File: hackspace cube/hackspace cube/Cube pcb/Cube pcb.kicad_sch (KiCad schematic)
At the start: 57 parts, among them J1 Conn_01x08 ( conector 1), J2 Conn_01x08 ( conector 2), J3 Conn_01x02 ( exstra ground co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, J4 Conn_01x14 ( Spare Ports ), Q1 BSS138, Q10 BSS138, Q11 BSS138, Q12 BSS138, Q13 BSS138, Q14 BSS138, Q15 BSS138, Q16 BSS138, Q2 BSS138, Q3 BSS138, Q4 BSS138, Q5 BSS138, Q6 BSS138, Q7 BSS138, Q8 BSS138, Q9 BSS138

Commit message: update
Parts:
- C1, C2, C3, C4: footprint Capacitor_SMD:C_0805_2012Metric -> (none)
- J1, J2: footprint Connector_PinHeader_2.54mm:PinHeader_1x08_P2.54mm_Vertical -> (none)
- J3: footprint Connector_PinHeader_2.54mm:PinHeader_1x02_P2.54mm_Vertical -> (none)
- J4: footprint Connector_PinHeader_2.54mm:PinHeader_1x14_P2.54mm_Vertical -> (none)
- R1, R10, R11, R12, R13, R14, R15, R16, R17, R18, R19, R2, R20, R21, R22, R23, R24, R25, R26, R27, R28, R29, R3, R30, R31, R32, R4, R5, R6, R7, R8, R9: footprint Resistor_SMD:R_0805_2012Metric -> (none)
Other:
- note added: "1.2"
- note removed: "1.1"
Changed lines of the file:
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@@
 		)
 	)
-	(text "1.1\n"
+	(text "1.2\n"
 		(exclude_from_sim no)
 		(at 270.256 193.294 0)
@@
 			)
 		)
-		(property "Footprint" "Capacitor_SMD:C_0805_2012Metric"
+		(property "Footprint" ""
 			(at 145.7452 41.91 0)
 			(effects
@@
 			)
 		)
-		(property "Footprint" "Capacitor_SMD:C_0805_2012Metric"
+		(property "Footprint" ""
 			(at 131.7752 41.91 0)
 			(effects
@@
 			)
 		)
-		(property "Footprint" "Resistor_SMD:R_0805_2012Metric"
+		(property "Footprint" ""
 			(at 24.892 163.83 90)
 			(effects
@@
 			)
 		)
-		(property "Footprint" "Resistor_SMD:R_0805_2012Metric"
+		(property "Footprint" ""
 			(at 45.212 163.83 90)
 			(effects
@@
 			)
 		)
-		(property "Footprint" "Resistor_SMD:R_0805_2012Metric"
+		(property "Footprint" ""
 			(at 51.562 26.67 90)
 			(effects
@@
 			)
 		)
-		(property "Footprint" "Connector_PinHeader_2.54mm:PinHeader_1x08_P2.54mm_Vertical"
+		(property "Footprint" ""
 			(at 162.56 85.09 0)
 			(effects
@@
 			)
 		)
-		(property "Footprint" "Connector_PinHeader_2.54mm:PinHeader_1x14_P2.54mm_Vertical"
+		(property "Footprint" ""
 			(at 248.92 135.89 0)
 			(effects
@@
 			)
 		)
-		(property "Footprint" "Resistor_SMD:R_0805_2012Metric"
+		(property "Footprint" ""
 			(at 68.072 88.9 90)
 			(effects
@@
 			)
 		)
-		(property "Footprint" "Resistor_SMD:R_0805_2012Metric"
+		(property "Footprint" ""
 			(at 51.562 44.45 90)
 			(effects
@@
 			)
 		)
-		(property "Footprint" "Resistor_SMD:R_0805_2012Metric"
+		(property "Footprint" ""
 			(at 31.242 44.45 90)
 			(effects
@@
 			)
 		)
-		(property "Footprint" "Connector_PinHeader_2.54mm:PinHeader_1x02_P2.54mm_Vertical"
+		(property "Footprint" ""
 			(at 163.83 144.78 0)
 			(effects
@@
 			)
 		)
-		(property "Footprint" "Resistor_SMD:R_0805_2012Metric"
+		(property "Footprint" ""
 			(at 89.662 26.67 90)
 			(effects
@@
 			)
 		)
-		(property "Footprint" "Resistor_SMD:R_0805_2012Metric"
+		(property "Footprint" ""
 			(at 29.972 134.62 90)
 			(effects
@@
 			)
 		)
-		(property "Footprint" "Resistor_SMD:R_0805_2012Metric"
+		(property "Footprint" ""
 			(at 87.122 88.9 90)
 			(effects
@@
 			)
 		)
-		(property "Footprint" "Resistor_SMD:R_0805_2012Metric"
+		(property "Footprint" ""
 			(at 49.022 88.9 90)
 			(effects
@@
 			)
 		)
-		(property "Footprint" "Resistor_SMD:R_0805_2012Metric"
+		(property "Footprint" ""
 			(at 65.532 181.61 90)
 			(effects
@@
 			)
 		)
-		(property "Footprint" "Resistor_SMD:R_0805_2012Metric"
+		(property "Footprint" ""
 			(at 87.122 134.62 90)
 			(effects
@@
 			)
 		)
-		(property "Footprint" "Resistor_SMD:R_0805_2012Metric"
+		(property "Footprint" ""
 			(at 29.972 116.84 90)
 			(effects
@@
 			)
 		)
-		(property "Footprint" "Resistor_SMD:R_0805_2012Metric"
+		(property "Footprint" ""
 			(at 68.072 116.84 90)
 			(effects
@@
 			)
 		)
-		(property "Footprint" "Resistor_SMD:R_0805_2012Metric"
+		(property "Footprint" ""
 			(at 84.582 181.61 90)
 			(effects
@@
 			)
 		)
-		(property "Footprint" "Resistor_SMD:R_0805_2012Metric"
+		(property "Footprint" ""
 			(at 49.022 71.12 90)
 			(effects
@@
 			)
 		)
-		(property "Footprint" "Resistor_SMD:R_0805_2012Metric"
+		(property "Footprint" ""
 			(at 29.972 88.9 90)
 			(effects
@@
 			)
 		)
-		(property "Footprint" "Resistor_SMD:R_0805_2012Metric"
+		(property "Footprint" ""
 			(at 49.022 134.62 90)
 			(effects
@@
 			)
 		)
-		(property "Footprint" "Resistor_SMD:R_0805_2012Metric"
+		(property "Footprint" ""
 			(at 84.582 163.83 90)
 			(effects
@@
 			)
 		)
-		(property "Footprint" "Resistor_SMD:R_0805_2012Metric"
+		(property "Footprint" ""
 			(at 49.022 116.84 90)
 			(effects
@@
 			)
 		)
-		(property "Footprint" "Capacitor_SMD:C_0805_2012Metric"
+		(property "Footprint" ""
 			(at 131.7752 67.31 0)
 			(effects
@@
 			)
 		)
-		(property "Footprint" "Resistor_SMD:R_0805_2012Metric"
+		(property "Footprint" ""
 			(at 87.122 71.12 90)
 			(effects
@@
 			)
 		)
-		(property "Footprint" "Resistor_SMD:R_0805_2012Metric"
+		(property "Footprint" ""
 			(at 89.662 44.45 90)
 			(effects
@@
 			)
 		)
-		(property "Footprint" "Resistor_SMD:R_0805_2012Metric"
+		(property "Footprint" ""
 			(at 65.532 163.83 90)
 			(effects
@@
 			)
 		)
-		(property "Footprint" "Resistor_SMD:R_0805_2012Metric"
+		(property "Footprint" ""
 			(at 29.972 71.12 90)
 			(effects
@@
 			)
 		)
-		(property "Footprint" "Resistor_SMD:R_0805_2012Metric"
+		(property "Footprint" ""
 			(at 70.612 44.45 90)
 			(effects
@@
 			)
 		)
-		(property "Footprint" "Connector_PinHeader_2.54mm:PinHeader_1x08_P2.54mm_Vertical"
+		(property "Footprint" ""
 			(at 162.56 113.03 0)
 			(effects
@@
 			)
 		)
-		(property "Footprint" "Resistor_SMD:R_0805_2012Metric"
+		(property "Footprint" ""
 			(at 70.612 26.67 90)
 			(effects
@@
 			)
 		)
-		(property "Footprint" "Resistor_SMD:R_0805_2012Metric"
+		(property "Footprint" ""
 			(at 45.212 181.61 90)
 			(effects
@@
 			)
 		)
-		(property "Footprint" "Resistor_SMD:R_0805_2012Metric"
+		(property "Footprint" ""
 			(at 87.122 116.84 90)
 			(effects
@@
 			)
 		)
-		(property "Footprint" "Resistor_SMD:R_0805_2012Metric"
+		(property "Footprint" ""
 			(at 24.892 181.61 90)
 			(effects
@@
 			)
 		)
-		(property "Footprint" "Capacitor_SMD:C_0805_2012Metric"
+		(property "Footprint" ""
 			(at 145.7452 67.31 0)
 			(effects
@@
 			)
 		)
-		(property "Footprint" "Resistor_SMD:R_0805_2012Metric"
+		(property "Footprint" ""
 			(at 68.072 134.62 90)
 			(effects
@@
 			)
 		)
-		(property "Footprint" "Resistor_SMD:R_0805_2012Metric"
+		(property "Footprint" ""
 			(at 68.072 71.12 90)
 			(effects
@@
 			)
 		)
-		(property "Footprint" "Resistor_SMD:R_0805_2012Metric"
+		(property "Footprint" ""
 			(at 31.242 26.67 90)
 			(effects

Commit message: pcb first draft
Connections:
- net 3V3_EN: now also J4.2 (Pin_2); no longer J4.3 (Pin_3)
- net ADC_VREF: now also J4.3 (Pin_3); no longer J4.14 (Pin_14)
- net GPIO-16: now also J4.14 (Pin_14); no longer J4.10 (Pin_10)
- net GPIO-17: now also J4.13 (Pin_13); no longer J4.9 (Pin_9)
- net GPIO-18: now also J4.12 (Pin_12); no longer J4.8 (Pin_8)
- net GPIO-19: now also J4.11 (Pin_11); no longer J4.7 (Pin_7)
- net GPIO-20: now also J4.10 (Pin_10); no longer J4.6 (Pin_6)
- net GPIO-21: now also J4.9 (Pin_9); no longer J4.5 (Pin_5)
- net GPIO-22: now also J4.8 (Pin_8); no longer J4.4 (Pin_4)
- net GPIO-26: now also J4.6 (Pin_6); no longer J4.13 (Pin_13)
- net GPIO-27: now also J4.5 (Pin_5); no longer J4.12 (Pin_12)
- net GPIO-28: now also J4.4 (Pin_4); no longer J4.11 (Pin_11)
- net RUN: now also J4.7 (Pin_7); no longer J4.2 (Pin_2)

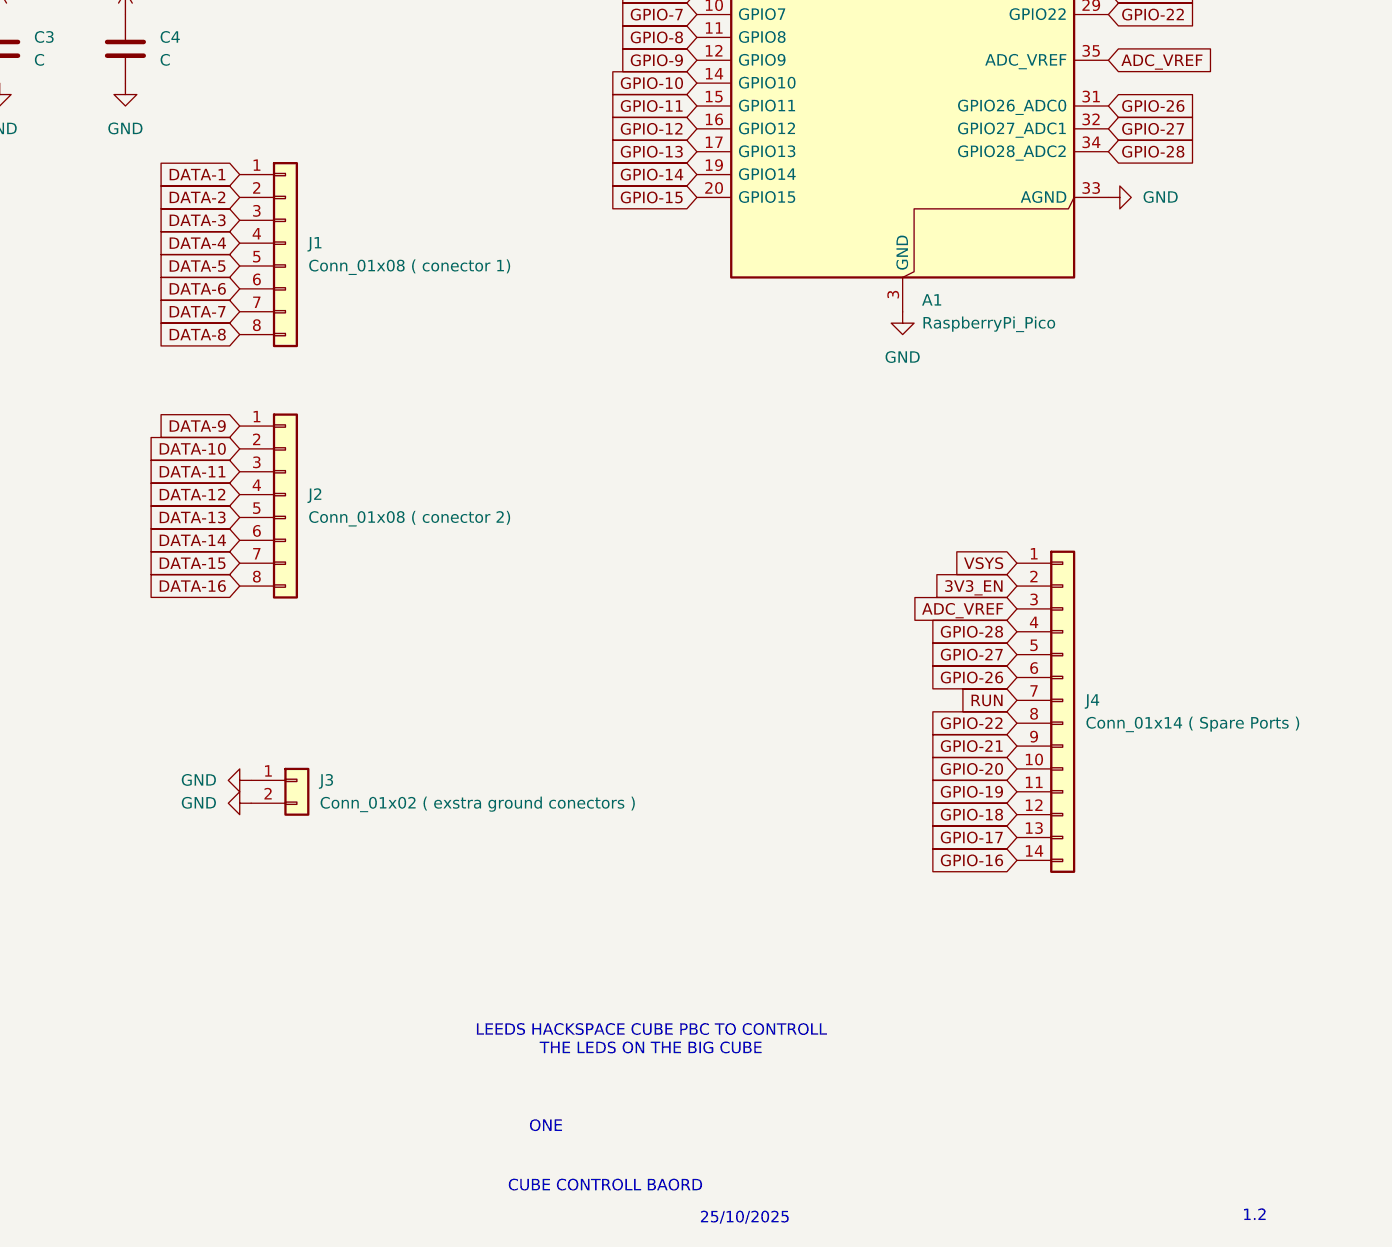
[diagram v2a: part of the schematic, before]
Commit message: updated wiring D and PCB
 wiring D now has GND on the connector pins . PCB now has new shorter design to make it 10cm wide just need to add ground plain
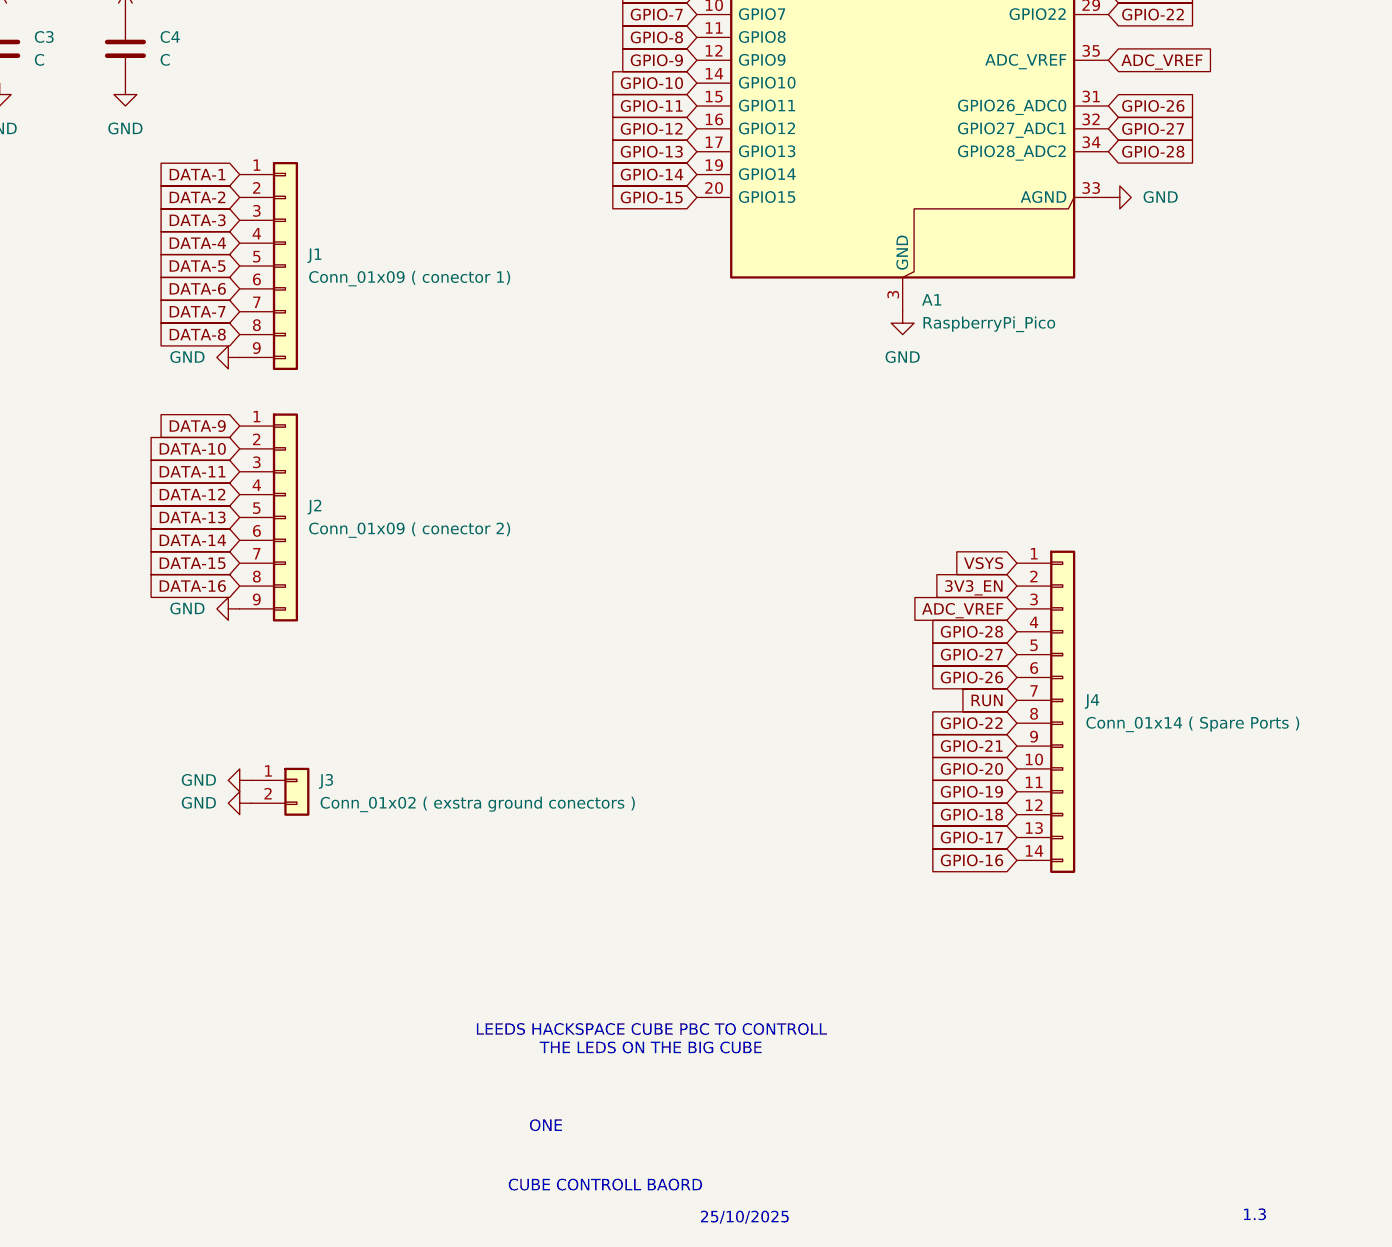
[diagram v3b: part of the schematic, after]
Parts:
- removed J1: Conn_01x08 ( conector 1), symbol Connector_Generic:Conn_01x08
- removed J2: Conn_01x08 ( conector 2), symbol Connector_Generic:Conn_01x08
- added J1: Conn_01x09 ( conector 1), Connector_PinHeader_2.54mm:PinHeader_1x09_P2.54mm_Vertical, symbol Connector_Generic:Conn_01x09
- added J2: Conn_01x09 ( conector 2), Connector_PinHeader_2.54mm:PinHeader_1x09_P2.54mm_Vertical, symbol Connector_Generic:Conn_01x09
- C1, C2, C3, C4: footprint (none) -> Capacitor_SMD:C_0805_2012Metric
- J3: footprint (none) -> Connector_PinHeader_2.54mm:PinHeader_1x02_P2.54mm_Vertical
- J4: footprint (none) -> Connector_PinHeader_2.54mm:PinHeader_1x14_P2.54mm_Vertical
- R1, R10, R11, R12, R13, R14, R15, R16, R17, R18, R19, R2, R20, R21, R22, R23, R24, R25, R26, R27, R28, R29, R3, R30, R31, R32, R4, R5, R6, R7, R8, R9: footprint (none) -> Resistor_SMD:R_0805_2012Metric
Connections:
- net DATA-1: now also J1.1 (Pin_1)
- net DATA-10: now also J2.2 (Pin_2)
- net DATA-11: now also J2.3 (Pin_3)
- net DATA-12: now also J2.4 (Pin_4)
- net DATA-13: now also J2.5 (Pin_5)
- net DATA-14: now also J2.6 (Pin_6)
- net DATA-15: now also J2.7 (Pin_7)
- net DATA-16: now also J2.8 (Pin_8)
- net DATA-2: now also J1.2 (Pin_2)
- net DATA-3: now also J1.3 (Pin_3)
- net DATA-4: now also J1.4 (Pin_4)
- net DATA-5: now also J1.5 (Pin_5)
- net DATA-6: now also J1.6 (Pin_6)
- net DATA-7: now also J1.7 (Pin_7)
- net DATA-8: now also J1.8 (Pin_8)
- net DATA-9: now also J2.1 (Pin_1)
- net GND: now also J1.9 (Pin_9), J2.9 (Pin_9)
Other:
- note added: "1.3"
- note removed: "1.2"
